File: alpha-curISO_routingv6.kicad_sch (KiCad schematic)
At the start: 27 parts, among them J2 SWD, Q1 2N2222, U1 RP2040, U5 74AHCT1G125

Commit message: simplified speaker mechanic
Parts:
- added LS1: Speaker, Keebio-Parts:AST1109MLTRQ, symbol Device:Speaker
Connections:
- net Audio: now also LS1.1
- net GND: now also LS1.2
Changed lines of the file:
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@@
+    )
+  )
+  (global_label "Audio" (shape input) (at 196.85 179.705 180) (fields_autoplaced)
+    (effects (font (size 1.27 1.27)) (justify right))
+    (property "Intersheet References" "${INTERSHEET_REFS}" (id 0) (at 189.2964 179.6256 0)
+      (effects (font (size 1.27 1.27)) (justify right) hide)
     )
   )
@@
     (pin "2")
   )
+  (symbol (lib_id "Device:Speaker") (at 201.93 179.705 0) (unit 1)
+    (in_bom yes) (on_board yes) (fields_autoplaced)
+    (property "Reference" "LS1" (id 0) (at 206.375 179.7049 0)
+      (effects (font (size 1.27 1.27)) (justify left))
+    )
+    (property "Value" "Speaker" (id 1) (at 206.375 182.2449 0)
+      (effects (font (size 1.27 1.27)) (justify left))
+    )
+    (property "Footprint" "Keebio-Parts:AST1109MLTRQ" (id 2) (at 201.93 184.785 0)
+      (effects (font (size 1.27 1.27)) hide)
+    )
+    (property "Datasheet" "~" (id 3) (at 201.676 180.975 0)
+      (effects (font (size 1.27 1.27)) hide)
+    )
+    (pin "1")
+    (pin "2")
+  )
   (symbol (lib_id "Device:R_Small") (at 116.205 189.865 90) (unit 1)
     (in_bom yes) (on_board yes) (fields_autoplaced)
@@
     (pin "3")
     (pin "4")
+  )
+  (symbol (lib_name "GND_2") (lib_id "power:GND") (at 196.85 182.245 0) (unit 1)
+    (in_bom yes) (on_board yes) (fields_autoplaced)
+    (property "Reference" "#PWR0151" (id 0) (at 196.85 188.595 0)
+      (effects (font (size 1.27 1.27)) hide)
+    )
+    (property "Value" "GND" (id 1) (at 196.85 186.69 0))
+    (property "Footprint" "" (id 2) (at 196.85 182.245 0)
+      (effects (font (size 1.27 1.27)) hide)
+    )
+    (property "Datasheet" "" (id 3) (at 196.85 182.245 0)
+      (effects (font (size 1.27 1.27)) hide)
+    )
+    (pin "1")
   )
   (sheet (at 287.655 26.67) (size 71.755 55.88) (fields_autoplaced)
@@
       (reference "#PWR0150") (unit 1) (value "GND") (footprint "")
     )
+    (path "/f1d52626-0ef9-449f-9220-adf121581ba9"
+      (reference "#PWR0151") (unit 1) (value "GND") (footprint "")
+    )
     (path "/cbaab640-727d-4334-9640-ed8234100729"
       (reference "#PWR0153") (unit 1) (value "+5V") (footprint "")
@@
       (reference "LED11") (unit 1) (value "YS-SK6812MINI-E") (footprint "CrumpPrints:WS2812-2020")
     )
+    (path "/be136826-5abb-42ef-a18a-702f84b0b1ce"
+      (reference "LS1") (unit 1) (value "Speaker") (footprint "Keebio-Parts:AST1109MLTRQ")
+    )
     (path "/e3fed552-2210-4413-aff9-5999ddf336e6"

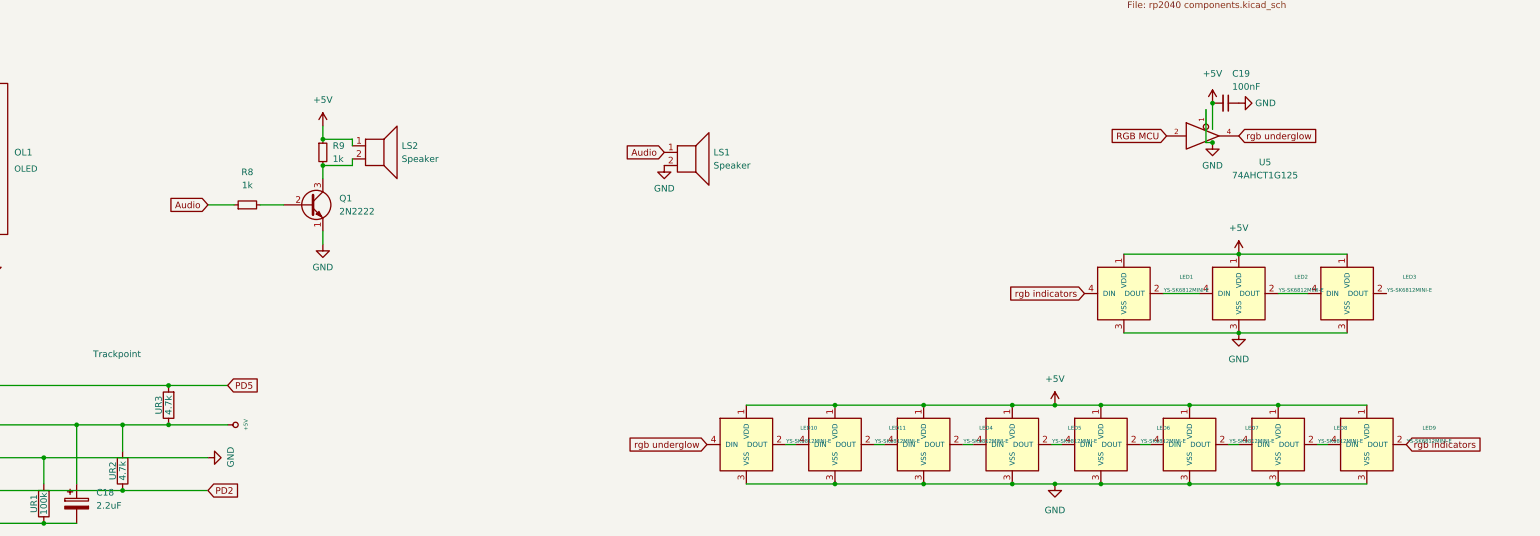
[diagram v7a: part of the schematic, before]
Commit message: added 4 more leds for underglow
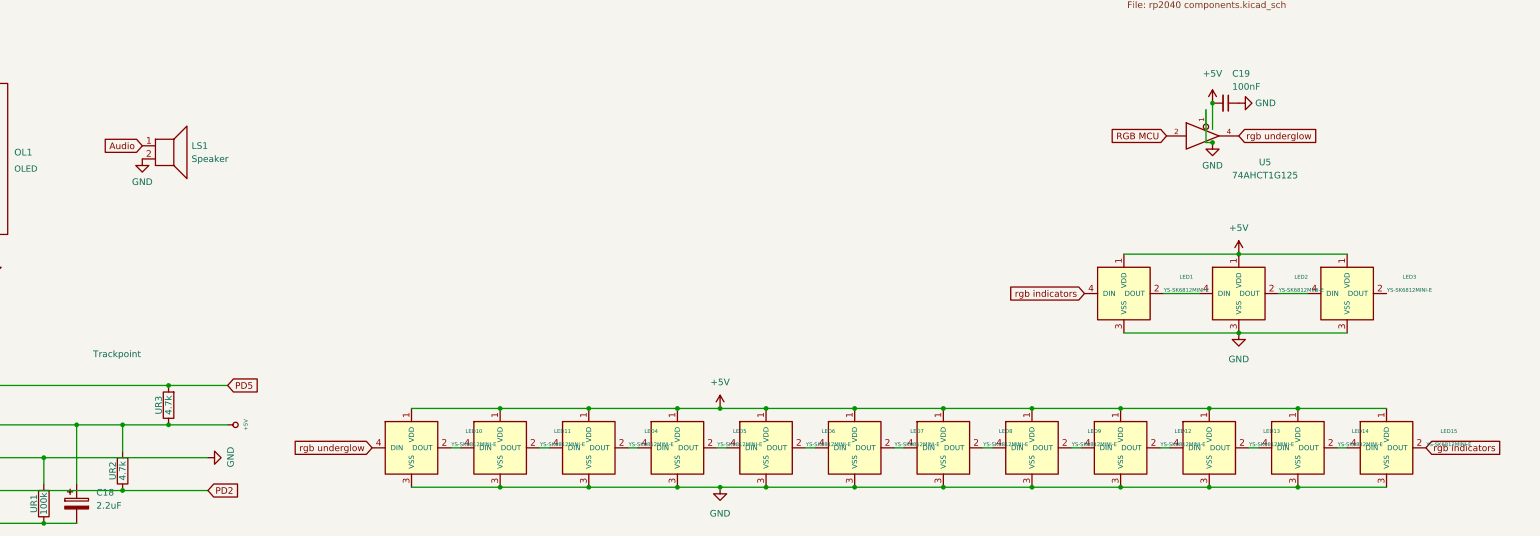
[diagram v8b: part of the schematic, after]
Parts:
- removed LS2: Speaker, Keebio-Parts:AST1109MLTRQ, symbol Device:Speaker
- removed Q1: 2N2222, Package_TO_SOT_SMD:SOT-23, symbol Transistor_BJT:2N2219
- removed R8: 1k, Keebio-Parts:Diode-Hybrid-Back, symbol Device:R_Small
- removed R9: 1k, Resistor_SMD:R_0402_1005Metric, symbol Device:R_Small
- added LED12, LED13, LED14, LED15: YS-SK6812MINI-E, CrumpPrints:WS2812-2020, symbol kbd:YS-SK6812MINI-E
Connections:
- net +5V: now also LED12.1 (VDD), LED13.1 (VDD), LED14.1 (VDD), LED15.1 (VDD)
- net GND: now also LED12.3 (VSS), LED13.3 (VSS), LED14.3 (VSS), LED15.3 (VSS)
- net rgb indicators: now also LED15.2 (DOUT); no longer LED9.2 (DOUT)
- new net: LED13.2 (DOUT), LED14.4 (DIN)
- new net: LED12.2 (DOUT), LED13.4 (DIN)
- new net: LED12.4 (DIN), LED9.2 (DOUT)
- new net: LED14.2 (DOUT), LED15.4 (DIN)
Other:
- moved on the sheet: LED10, LED11, LED4, LED5, LED6, LED7, LED8, LED9, LS1
